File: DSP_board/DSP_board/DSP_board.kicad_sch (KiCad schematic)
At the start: 59 parts

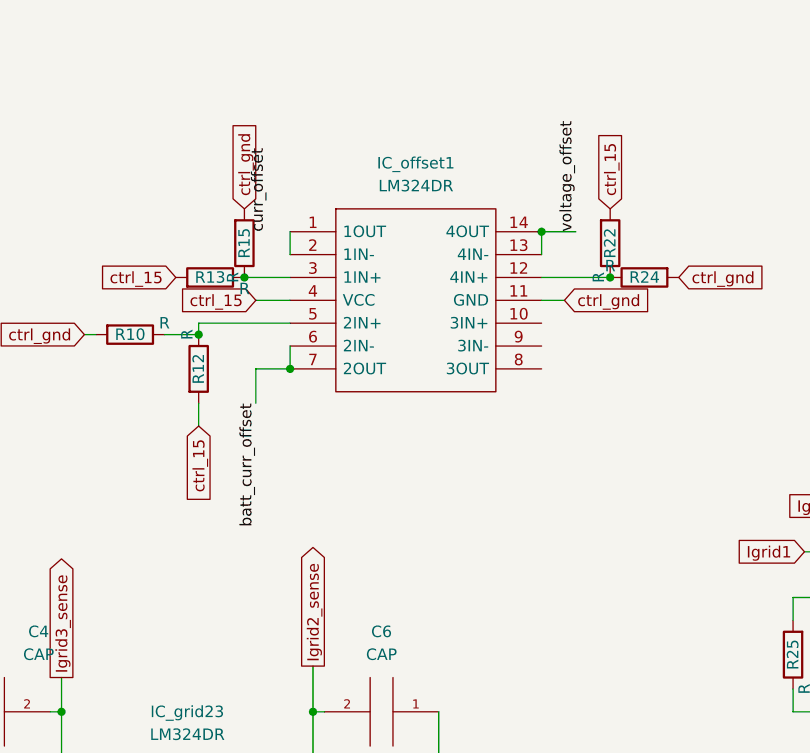
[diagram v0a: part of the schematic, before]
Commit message: adding offset measurements
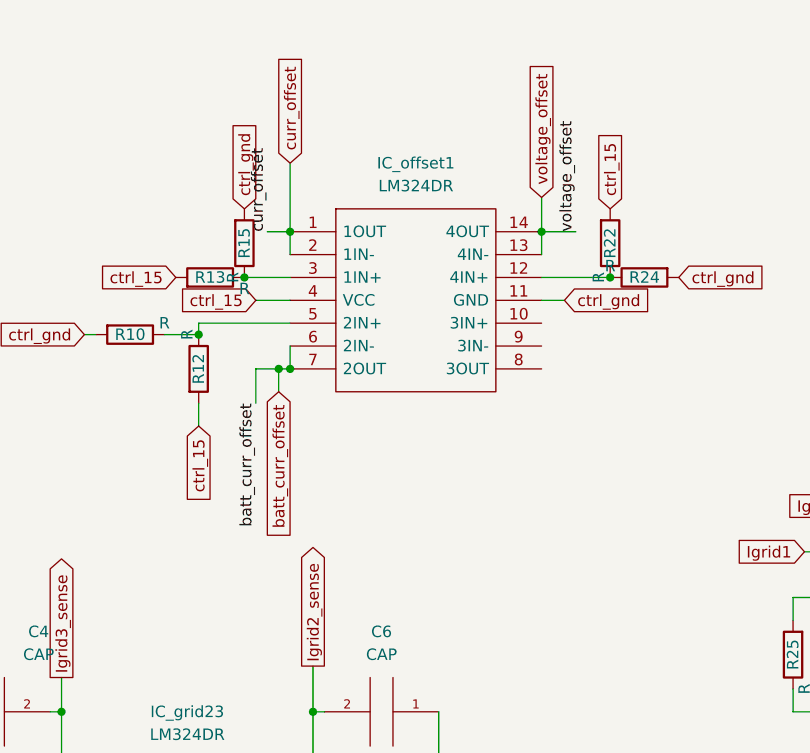
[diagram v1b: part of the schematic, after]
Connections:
- net curr_offset: now also IC_offset1.1 (1OUT), IC_offset1.2 (1IN-)
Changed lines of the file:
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@@
   (junction (at 80.01 63.5) (diameter 0) (color 0 0 0 0)
   )
+  (junction (at 88.9 67.31) (diameter 0) (color 0 0 0 0)
+  )
   (junction (at 93.98 128.27) (diameter 0) (color 0 0 0 0)
   )
@@
   (junction (at 50.8 138.43) (diameter 0) (color 0 0 0 0)
   )
-  (wire (pts (xy 86.36 67.31) (xy 90.17 67.31))
+  (junction (at 90.17 52.07) (diameter 0) (color 0 0 0 0)
+  )
+  (wire (pts (xy 86.36 67.31) (xy 88.9 67.31))
     (stroke (width 0) (type default) (color 0 0 0 0))
   )
@@
     (stroke (width 0) (type default) (color 0 0 0 0))
   )
+  (wire (pts (xy 118.11 48.26) (xy 118.11 52.07))
+    (stroke (width 0) (type default) (color 0 0 0 0))
+  )
   (wire (pts (xy 369.57 90.17) (xy 367.03 90.17))
     (stroke (width 0) (type default) (color 0 0 0 0))
@@
     (stroke (width 0) (type default) (color 0 0 0 0))
   )
+  (wire (pts (xy 90.17 44.45) (xy 90.17 52.07))
+    (stroke (width 0) (type default) (color 0 0 0 0))
+  )
   (wire (pts (xy 227.33 109.22) (xy 231.14 109.22))
     (stroke (width 0) (type default) (color 0 0 0 0))
@@
     (stroke (width 0) (type default) (color 0 0 0 0))
   )
+  (wire (pts (xy 87.63 52.07) (xy 90.17 52.07))
+    (stroke (width 0) (type default) (color 0 0 0 0))
+  )
   (wire (pts (xy 200.66 173.99) (xy 220.98 173.99))
     (stroke (width 0) (type default) (color 0 0 0 0))
@@
     (stroke (width 0) (type default) (color 0 0 0 0))
   )
+  (wire (pts (xy 88.9 69.85) (xy 88.9 67.31))
+    (stroke (width 0) (type default) (color 0 0 0 0))
+  )
   (wire (pts (xy 59.69 123.19) (xy 64.77 123.19))
     (stroke (width 0) (type default) (color 0 0 0 0))
@@
   )
   (wire (pts (xy 40.64 138.43) (xy 38.1 138.43))
+    (stroke (width 0) (type default) (color 0 0 0 0))
+  )
+  (wire (pts (xy 88.9 67.31) (xy 90.17 67.31))
     (stroke (width 0) (type default) (color 0 0 0 0))
   )
@@
     )
   )
+  (global_label "curr_offset" (shape input) (at 90.17 44.45 90) (fields_autoplaced)
+    (effects (font (size 1.27 1.27)) (justify left))
+    (property "Intersheet References" "${INTERSHEET_REFS}" (id 0) (at 90.0906 31.8164 90)
+      (effects (font (size 1.27 1.27)) (justify left) hide)
+    )
+  )
   (global_label "ctrl_-15" (shape input) (at 143.51 200.66 180) (fields_autoplaced)
     (effects (font (size 1.27 1.27)) (justify right))
@@
     )
   )
+  (global_label "batt_curr_offset" (shape input) (at 88.9 69.85 270) (fields_autoplaced)
+    (effects (font (size 1.27 1.27)) (justify right))
+    (property "Intersheet References" "${INTERSHEET_REFS}" (id 0) (at 88.8206 87.2007 90)
+      (effects (font (size 1.27 1.27)) (justify right) hide)
+    )
+  )
   (global_label "curr_leakeage_i" (shape input) (at 353.06 82.55 180) (fields_autoplaced)
     (effects (font (size 1.27 1.27)) (justify right))
@@
       (effects (font (size 1.27 1.27)) (justify left) hide)
     )
+  )
+  (global_label "voltage_offset" (shape input) (at 118.11 48.26 90) (fields_autoplaced)
+    (effects (font (size 1.27 1.27)) (justify left))
+    (property "Intersheet References" "${INTERSHEET_REFS}" (id 0) (at 118.0306 32.5421 90)
+      (effects (font (size 1.27 1.27)) (justify left) hide)
+    )

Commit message: controller_final
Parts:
- removed C12, C13, C5, C6, C8: CAP, Capacitor_SMD:C_1206_3216Metric_Pad1.33x1.80mm_HandSolder, symbol pspice:CAP
- removed IC_batt1: LM358S-13, SOIC127P600X175-8N, symbol LM324:LM358S-13
- removed JDAB_batt1, JDAB_dclink1: Conn_02x04_Odd_Even, Connector_PinSocket_2.54mm:PinSocket_2x04_P2.54mm_Vertical, symbol Connector_Generic:Conn_02x04_Odd_Even
- removed JVSI1: Conn_02x08_Odd_Even, Connector_PinSocket_2.54mm:PinSocket_2x08_P2.54mm_Vertical, symbol Connector_Generic:Conn_02x08_Odd_Even
- removed R10, R11, R12, R14, R17, R18, R20, R22, R24, R27, R30, R31, R34, R9: R, Resistor_SMD:R_1206_3216Metric_Pad1.30x1.75mm_HandSolder, symbol Device:R
- added J7: Conn_02x10_Odd_Even, Connector_PinSocket_2.54mm:PinSocket_2x10_P2.54mm_Vertical, symbol Connector_Generic:Conn_02x10_Odd_Even
- added J8: Conn_02x06_Odd_Even, Connector_PinSocket_2.54mm:PinSocket_2x07_P2.54mm_Vertical, symbol Connector_Generic:Conn_02x06_Odd_Even
- added J9: Conn_02x06_Odd_Even, Connector_PinSocket_2.54mm:PinSocket_2x06_P2.54mm_Vertical, symbol Connector_Generic:Conn_02x06_Odd_Even
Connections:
- net Igrid3_ref is gone; now on an unnamed net: R4.2
- net batt_curr_1 is gone; now on an unnamed net: R8.2
- net DAB1PWM11: now also J9.5 (Pin_5)
- net DAB1PWM12: now also J9.6 (Pin_6)
- net DAB1PWM21: now also J9.3 (Pin_3)
- net DAB1PWM22: now also J9.4 (Pin_4)
- net DAB2_PWM11: now also J8.8 (Pin_8)
- net DAB2_PWM12: now also J8.6 (Pin_6)
- net DAB2_PWM21: now also J8.7 (Pin_7)
- net DAB2_PWM22: now also J8.5 (Pin_5)
- net I_leackage: now also IC_dclink_leakage1.13 (4IN-)
- net Igrid1: now also J7.5 (Pin_5)
- net Igrid1_sense: now also IC_dclink_leakage1.2 (1IN-)
- net Igrid2: now also J7.3 (Pin_3)
- net Igrid2_sense: now also IC_grid23.13 (4IN-)
- net Igrid3: now also J7.1 (Pin_1)
- net Igrid3_sense: now also IC_grid23.2 (1IN-); no longer C4.2
- net VSI11: now also J7.17 (Pin_17)
- net VSI12: now also J7.18 (Pin_18)
- net VSI21: now also J7.15 (Pin_15)
- net VSI22: now also J7.16 (Pin_16)
- net VSI31: now also J7.13 (Pin_13)
- net VSI32: now also J7.14 (Pin_14)
- net V_dc_link: now also J9.2 (Pin_2)
- net Vgrid1: now also J7.6 (Pin_6)
- net Vgrid2: now also J7.4 (Pin_4)
- net Vgrid3: now also J7.2 (Pin_2)
- net batt_V_sense: now also IC_offset1.8 (3OUT), IC_offset1.9 (3IN-)
- net batt_curr_0: now also J8.1 (Pin_1)
- net batt_curr_sense: now also IC_offset1.6 (2IN-), IC_offset1.7 (2OUT)
- net batt_v: now also R5.1, J8.2 (Pin_2)
- net ctrl_-15: now also IC_dclink_leakage1.11 (GND), IC_grid23.11 (GND), IC_offset1.11 (GND)
- net ctrl_gnd: now also C4.2, R8.1, J7.10 (Pin_10), J8.4 (Pin_4), J9.11 (Pin_11); no longer IC_dclink_leakage1.11 (GND), IC_grid23.11 (GND), IC_offset1.11 (GND)
- net curr_leakeage_i: now also J9.1 (Pin_1)
- net at C2.1, R2.1: now also IC_offset1.5 (2IN+); no longer R5.2
- net at IC_offset1.10 (3IN+): now also C4.1, R5.2
- removed net batt_curr_offset: C2.2, IC_offset1.6 (2IN-), IC_offset1.7 (2OUT), R5.1
- net curr_offset renamed offset_v
- net offset_v: now also C11.2, C2.2, C3.2, C7.2, R19.1, R28.1, R4.1, R6.1
- removed net voltage_offset: C11.2, C3.2, C7.2, IC_offset1.13 (4IN-), IC_offset1.14 (4OUT), R19.1, R28.1, R6.1
- new net OCD_grd2: J7.8 (Pin_8)
- new net OCD_grid1: J7.7 (Pin_7)
- new net OCD_grid3: J7.9 (Pin_9)
- new net OCD_leakage: J9.12 (Pin_12)
- new net SCL: J7.19 (Pin_19), J8.12 (Pin_12), J9.9 (Pin_9)
- new net SDA: J7.20 (Pin_20), J8.11 (Pin_11), J9.10 (Pin_10)
- new net batt_fault: J8.10 (Pin_10)
- new net batt_ready: J8.9 (Pin_9)
- new net dc_fault: J9.8 (Pin_8)
- new net dc_ready: J9.7 (Pin_7)
- new net vsi_fault: J7.12 (Pin_12)
- new net vsi_ready: J7.11 (Pin_11)
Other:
- moved on the sheet: IC_offset1, R13, R15
